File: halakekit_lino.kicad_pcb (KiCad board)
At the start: 2 copper layers, 33 x 19.3 mm, 10 parts, among them J1 HEADER_3, J2 HEADER_3, J3 HEADER_3, J4 HEADER_3, U1 BCM20737S

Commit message: Updated to ver1.1
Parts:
- C: renamed from 100u1; footprint Capacitors_SMD:C_0201 -> Capacitors_SMD:C_0603
- R: renamed from 10K1; footprint Resistors_SMD:R_0201 -> Resistors_SMD:R_0603
- moved G*** 23.5 mm to (152.3, 94.2)
- moved G*** 1.68 mm to (164.1, 110.9)
- moved J1 1.27 mm to (153.9, 109.7), turned to 270 degrees
- moved J2 1.27 mm to (179.3, 109.7), turned to 270 degrees
- moved J3 1.27 mm to (174.3, 112.2), turned to 90 degrees
- moved J4 1.27 mm to (148.9, 112.2), turned to 90 degrees
- moved R 1.17 mm to (149.5, 98.3)
- moved C 0.71 mm to (149.5, 95.3)
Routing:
- net GND: track 85.6 -> 115.3 mm, vias 4 -> 7
- net VCC: track 56.4 -> 73.2 mm, vias 3 -> 5
- net RST: track 13.6 -> 17.7 mm
- net RX: track 17.1 -> 20.9 mm
- net AIO: track 34.0 -> 37.6 mm
- net TX: track 19.9 -> 22.4 mm
- net PIO0: track 34.4 -> 33.1 mm
- net Net-(10K1-Pad2): track 10.9 -> 11.4 mm
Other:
- board size 33 x 19.3 mm -> 33 x 20.6 mm
- net class Default: trace_width 3 -> 0.1; via_dia 0.6 -> 0.5
- board text added: "CR2032"
- board text added: "ver.1.1"
- board text removed: "ver.1.0"

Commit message: Add files to order PCBA for elecrow
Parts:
- C: footprint Capacitors_SMD:C_0603 -> register_and_condensor:C_0603
- R: footprint Resistors_SMD:R_0603 -> register_and_condensor:R_0603
- moved G*** 0.24 mm to (152.4, 94.4)
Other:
- outline, holes or cut-outs redrawn
- board text added: "BCM20737S"

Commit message: Change board layout as rev 1.2
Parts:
- removed the G*** at (164.1, 110.9)
- removed J2, J3, J4: HEADER_3, simple_headers:Pin_Header_Straight_1x03_circle
- added G***: LOGO, osh-logo:osh-logo-4p3mm, F.Cu at (177.3, 100.8)
- added G***: LOGO, osh-logo:osh-logo-4p3mm, F.Cu at (174.5, 99.2)
- added G***: LOGO, osh-logo:osh-logo-3p4mm, F.Cu at (167.2, 95.2)
- added G***: LOGO, osh-logo:osh-logo-3p4mm, B.Cu at (167.4, 104.1)
- added G***: LOGO, logos:nyampass_logo_8p4mm, F.Cu at (165.1, 106.9)
- BT1: footprint CR2032_frame:BC-2001(CR2032 frame) -> CR2032_frame:BAT-HLD-001-TRCT
- J1: value HEADER_3 -> HEADER_10; footprint simple_headers:Pin_Header_Straight_1x03_circle -> simple_headers:Pin_Header_Straight_1x10
- moved G*** 17.9 mm to (165.1, 107.0), turned to 0 degrees
- moved J1 8.82 mm to (145.3, 111.4), turned to 90 degrees
- moved BT1 7.13 mm to (156.7, 98.5)
- moved R 2.24 mm to (148.5, 96.3), turned to 0 degrees
- moved C 1.31 mm to (148.5, 94.4), turned to 0 degrees
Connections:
- J1 pad 1: RST -> FWTX
- J1 pad 2: RX -> FWRX
- J1 pad 3: TX -> VCC
- U1 pad 1: PIO1 -> D1
- U1 pad 18: RX -> FWRX
- U1 pad 19: TX -> FWTX
- U1 pad 27: RST -> Net-(U1-Pad27)
- U1 pad 28: Net-(U1-Pad28) -> TX
- U1 pad 31: Net-(U1-Pad31) -> RX
- U1 pad 35: Net-(U1-Pad35) -> A1
- U1 pad 40: AIO -> A0
- U1 pad 42: PIO0 -> D0
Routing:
- net AIO: track 37.6 -> 0.00 mm, vias 1 -> 0
- net PIO1: track 33.7 -> 0.00 mm, vias 1 -> 0
- net PIO0: track 33.1 -> 0.00 mm, vias 1 -> 0
- net FWTX: track 0.00 -> 27.0 mm, vias 0 -> 1
- net D1: track 0.00 -> 25.2 mm, vias 0 -> 1
- net FWRX: track 0.00 -> 23.1 mm, vias 0 -> 1
- net D0: track 0.00 -> 18.4 mm, vias 0 -> 1
- net A1: track 0.00 -> 18.3 mm, vias 0 -> 1
- net RST: track 17.7 -> 0.00 mm, vias 1 -> 0
- net A0: track 0.00 -> 17.4 mm, vias 0 -> 1
- net VCC: track 73.2 -> 69.4 mm, vias 5 -> 3
- net TX: track 22.4 -> 23.6 mm
- net Net-(10K1-Pad2): track 11.4 -> 12.6 mm
- net GND: track 115.3 -> 115.4 mm, vias 7 -> 8
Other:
- board size 33 x 20.6 mm -> 25.5 x 20.1 mm
- net class GND added: clearance 0.1, trace_width 0.2, via_dia 0.5, via_drill 0.4
- net class VCC added: clearance 0.1, trace_width 0.2, via_dia 0.5, via_drill 0.4
- board text added: "A0 P14"
- board text added: "A1 P32"
- board text added: "D0 P26"
- board text added: "D1 D27"
- board text added: "D1 P27"
- board text added: "FW RX"
- board text added: "FW TX"
- board text added: "HaLakeKit"
- board text added: "Lino"
- board text added: "RX P2"
- board text added: "Rev 2.0"
- board text added: "TX P0"
- board text removed: "AIO0"
- board text removed: "BCM20737S"
- board text removed: "PIO0"
- board text removed: "PIO1"
- board text removed: "RST"
- board text removed: "RX"
- board text removed: "TX"
- board text removed: "ver.1.1"

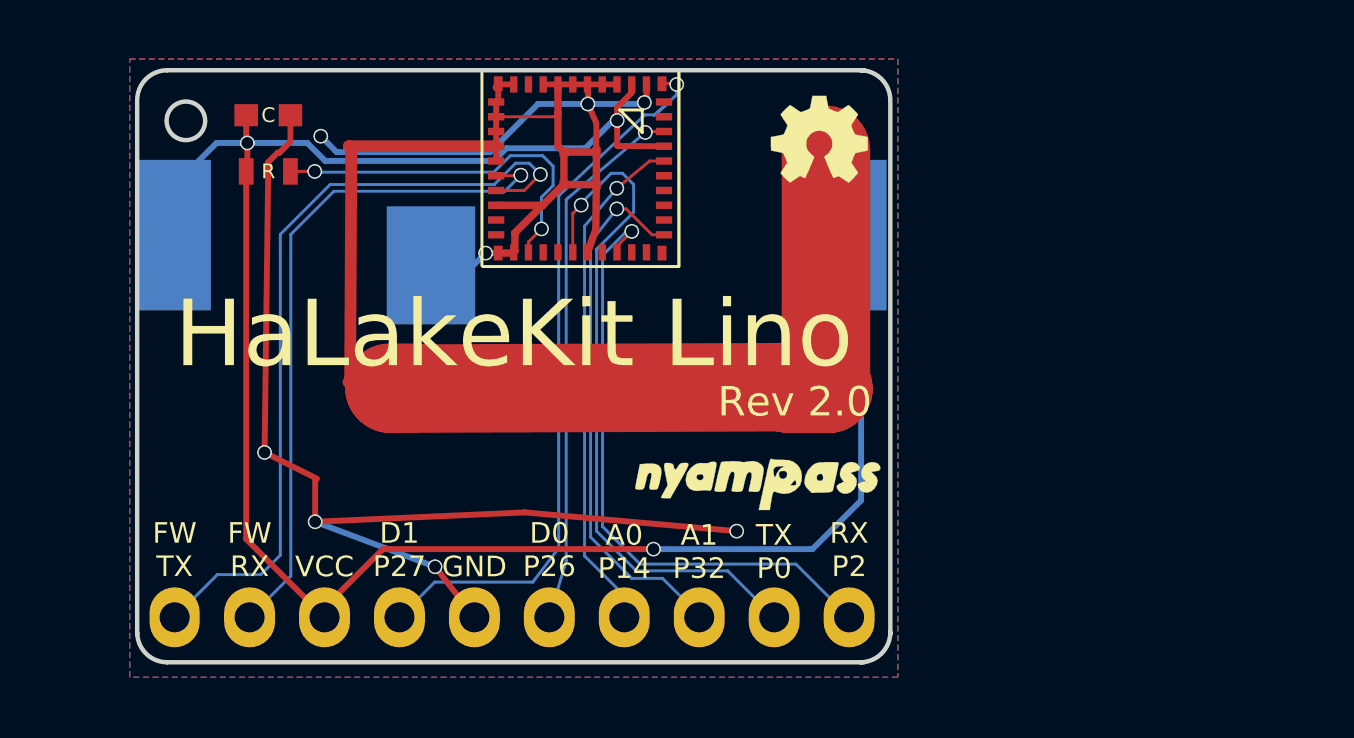
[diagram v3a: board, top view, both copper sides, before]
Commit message: Create net data with using MDBT40
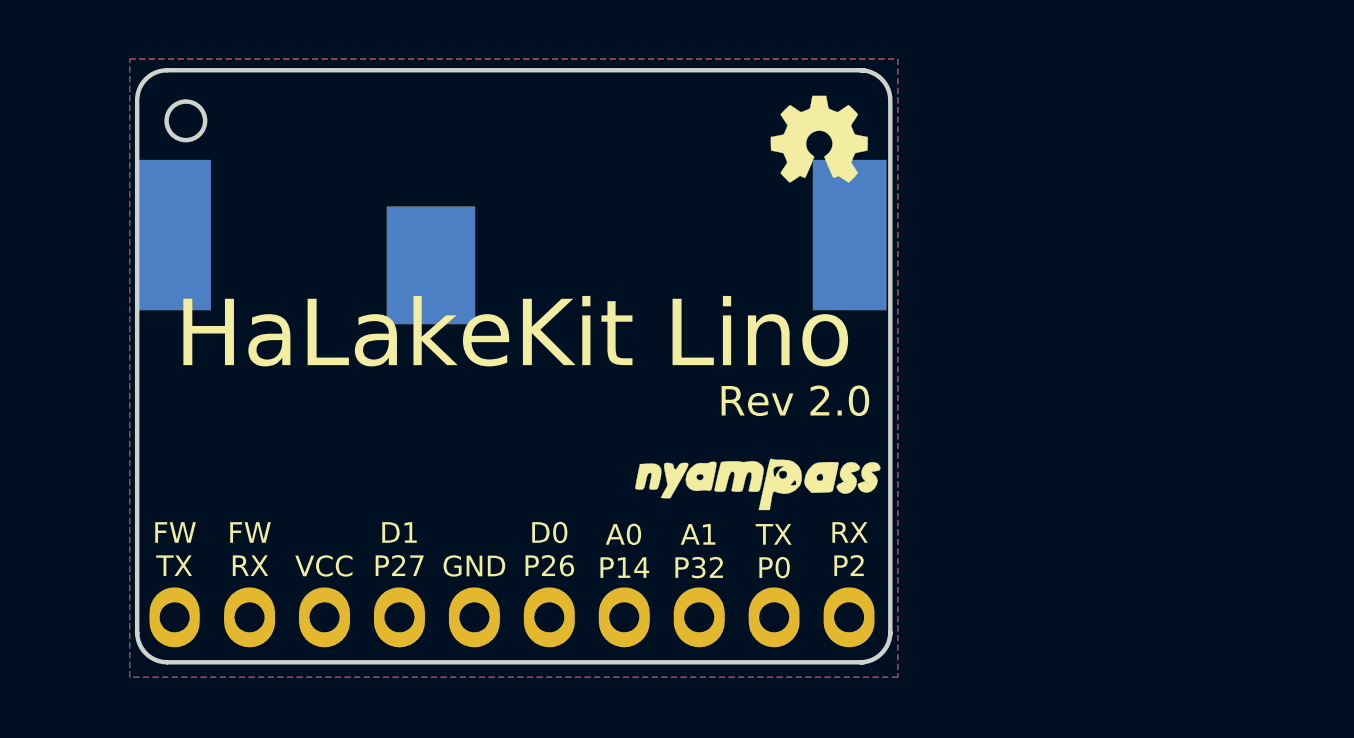
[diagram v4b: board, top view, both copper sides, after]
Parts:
- removed C: C, register_and_condensor:C_0603
- removed R: R, register_and_condensor:R_0603
- removed U1: BCM20737S, BCM20737S:BCM20737S
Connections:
- BT1 pad 1: VCC -> +3V3
- J1 pad 1: FWTX -> SWDCLK
- J1 pad 10: RX -> P4_Drain
- J1 pad 2: FWRX -> SWDIO
- J1 pad 3: VCC -> P0
- J1 pad 4: D1 -> P1
- J1 pad 6: D0 -> VCC
- J1 pad 7: A0 -> +3V3
- J1 pad 8: A1 -> P2
- J1 pad 9: TX -> P3
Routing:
- net GND: track 115.4 -> 1.44 mm, vias 8 -> 0
- net VCC: track 69.4 -> 0.00 mm, vias 3 -> 0
- net FWTX: track 27.0 -> 0.00 mm, vias 1 -> 0
- net D1: track 25.2 -> 0.00 mm, vias 1 -> 0
- net TX: track 23.6 -> 0.00 mm, vias 1 -> 0
- net FWRX: track 23.1 -> 0.00 mm, vias 1 -> 0
- net RX: track 21.1 -> 0.00 mm, vias 1 -> 0
- net D0: track 18.4 -> 0.00 mm, vias 1 -> 0
- net A1: track 18.3 -> 0.00 mm, vias 1 -> 0
- net A0: track 17.4 -> 0.00 mm, vias 1 -> 0
- net Net-(10K1-Pad2): track 12.6 -> 0.00 mm, vias 2 -> 0
- net +3V3: track 0.00 -> 4.71 mm

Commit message: Update pcb to rev3.0
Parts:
- added C1: 12pf, register_and_condensor:C_0603, F.Cu at (167.9, 98.5)
- added C2: 12pf, register_and_condensor:C_0603, F.Cu at (161.3, 98.5)
- added C3: 0.01uf, register_and_condensor:C_0603, F.Cu at (152.2, 98.5)
- added C4: 4.7uf1, register_and_condensor:C_0603, F.Cu at (150.4, 98.5)
- added C5: 0.1uf1, register_and_condensor:C_0603, F.Cu at (159.5, 98.5)
- added R1: 1K, register_and_condensor:R_0603, F.Cu at (157.8, 98.5)
- added R2: 1K, register_and_condensor:R_0603, F.Cu at (148.4, 98.5)
- added U1: MDBT40, MDBT40:MDBT40, F.Cu at (165.1, 105.8)
- added U2: NJM2870, common:SOT-23-5, F.Cu at (155.0, 98.5)
- added U3: RTF015N03, mosfet:rtf015n03, F.Cu at (145.1, 98.5)
- added Y1: Crystal, common:FC-135, F.Cu at (164.6, 98.5)
- moved G*** 69.6 mm to (105.4, 107.4)
- moved G*** 69.6 mm to (108.2, 108.9)
- moved J1 28.5 mm to (168.2, 94.4), turned to 270 degrees
- moved G*** 21.1 mm to (146.3, 103.0), turned to 180 degrees
- moved G*** 18.4 mm to (148.6, 98.7), turned to 180 degrees
- moved G*** 14.3 mm to (151.0, 109.8)
- moved BT1 9.40 mm to (156.7, 107.9), turned to 180 degrees
- moved G*** 5.46 mm to (171.7, 98.2)
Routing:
- net +3V3: track 4.71 -> 45.3 mm, vias 0 -> 2
- net GND: track 1.44 -> 30.1 mm, vias 0 -> 9
- net SWDCLK: track 0.00 -> 17.8 mm, vias 0 -> 1
- net SWDIO: track 0.00 -> 16.8 mm, vias 0 -> 1
- net P3: track 0.00 -> 16.1 mm, vias 0 -> 1
- net P0: track 0.33 -> 15.9 mm, vias 0 -> 1
- net P1: track 0.00 -> 14.3 mm, vias 0 -> 1
- net P4: track 0.00 -> 14.2 mm
- net P2: track 0.08 -> 13.9 mm, vias 0 -> 1
- net Net-(C1-Pad1): track 0.00 -> 10.4 mm
- net VCC: track 0.00 -> 7.20 mm
- net Net-(C2-Pad1): track 0.00 -> 6.30 mm
- net Net-(R1-Pad2): track 0.00 -> 4.60 mm, vias 0 -> 2
- net P4_Drain: track 0.00 -> 4.17 mm
- net Net-(C3-Pad1): track 0.00 -> 1.78 mm
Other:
- board size 25.5 x 20.1 mm -> 30.1 x 20.1 mm
- net class GND removed
- net class Power added: clearance 0.1, trace_width 0.2, via_dia 0.5, via_drill 0.4
- net class VCC removed
- board text added: "3.3"
- board text added: "P0"
- board text added: "P1"
- board text added: "P2"
- board text added: "P3"
- board text added: "P4 Drain"
- board text added: "Rev 3.0"
- board text added: "SW CLK"
- board text added: "SW DIO"
- board text added: "github.com/nyampass/halakekit_lino_pcb"
- board text removed: "A0 P14"
- board text removed: "A1 P32"
- board text removed: "D0 P26"
- board text removed: "D1 D27"
- board text removed: "D1 P27"
- board text removed: "FW RX"
- board text removed: "FW TX"
- board text removed: "HaLakeKit Lino"
- board text removed: "RX P2"
- board text removed: "Rev 2.0"
- board text removed: "TX P0"

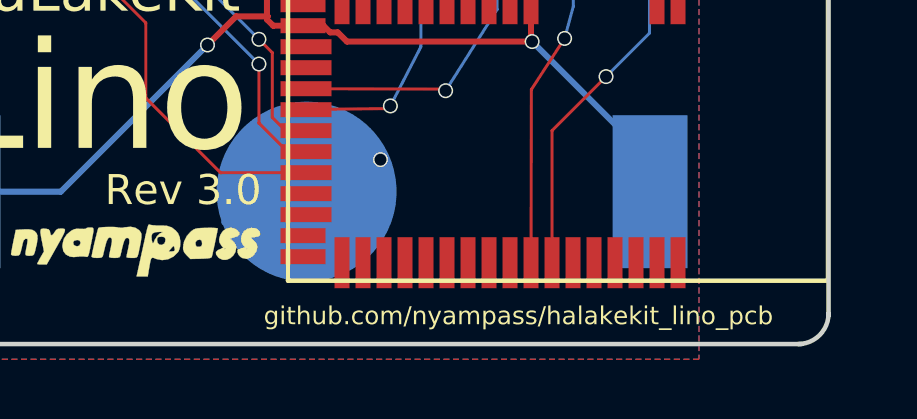
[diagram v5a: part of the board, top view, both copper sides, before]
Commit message: Change url on pcb
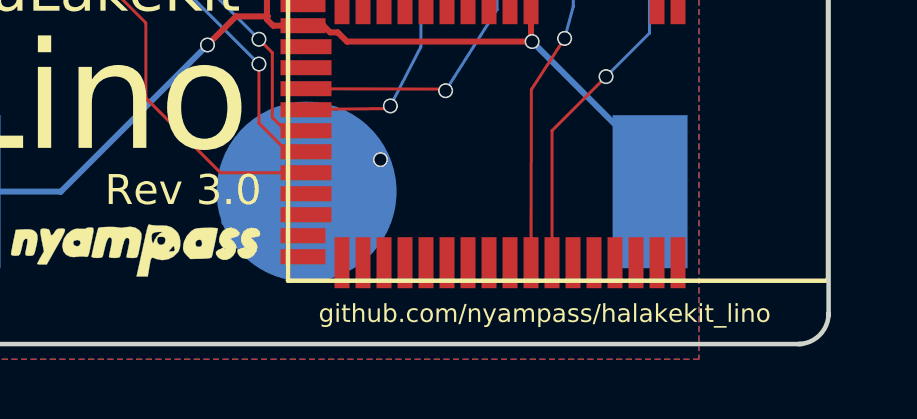
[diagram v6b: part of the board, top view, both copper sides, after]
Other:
- board text added: "github.com/nyampass/halakekit_lino"
- board text removed: "github.com/nyampass/halakekit_lino_pcb"
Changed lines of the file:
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@@
     (effects (font (size 0.7 0.7) (thickness 0.125)) (justify mirror))
   )
-  (gr_text github.com/nyampass/halakekit_lino_pcb (at 163.8046 112.014) (layer F.SilkS)
+  (gr_text github.com/nyampass/halakekit_lino (at 164.6809 111.9378) (layer F.SilkS)
     (effects (font (size 0.6 0.6) (thickness 0.15)))
   )
@@
   (segment (start 150.3934 99.2258) (end 149.8614 99.2258) (width 0.2) (layer F.Cu) (net 2))
   (segment (start 149.8614 99.2258) (end 148.3614 97.7258) (width 0.2) (layer F.Cu) (net 2))
-  (segment (start 145.2934 107.8738) (end 148.5519 107.8738) (width 0.2) (layer B.Cu) (net 13) (status 400000))
+  (segment (start 145.2934 107.8738) (end 148.5519 107.8738) (width 0.2) (layer B.Cu) (net 13))
   (segment (start 154.3939 102.0318) (end 155.4226 102.0318) (width 0.2) (layer F.Cu) (net 13))
   (segment (start 153.4414 102.9843) (end 154.3939 102.0318) (width 0.2) (layer F.Cu) (net 13))
@@
   (via (at 165.345207 102.765209) (size 0.5) (drill 0.4) (layers F.Cu B.Cu) (net 18))
   (segment (start 164.236313 104.4702) (end 165.345207 102.765209) (width 0.1) (layer F.Cu) (net 18))
-  (segment (start 156.1254 104.4418) (end 161.3251 104.4545) (width 0.1) (layer F.Cu) (net 19) (status 400000))
+  (segment (start 156.1254 104.4418) (end 161.3251 104.4545) (width 0.1) (layer F.Cu) (net 19))
   (segment (start 163.0934 101.8032) (end 163.0934 94.4118) (width 0.1) (layer B.Cu) (net 19))
   (segment (start 161.3789 104.5083) (end 163.0934 101.8032) (width 0.1) (layer B.Cu) (net 19))
   (via (at 161.3789 104.5083) (size 0.5) (drill 0.4) (layers F.Cu B.Cu) (net 19))
   (segment (start 161.3251 104.4545) (end 161.3789 104.5083) (width 0.1) (layer F.Cu) (net 19))
-  (segment (start 156.1254 105.1418) (end 159.45 105.1037) (width 0.1) (layer F.Cu) (net 20) (status 400000))
+  (segment (start 156.1254 105.1418) (end 159.45 105.1037) (width 0.1) (layer F.Cu) (net 20))
   (segment (start 160.5534 103.0478) (end 160.5534 94.4118) (width 0.1) (layer B.Cu) (net 20))
   (segment (start 159.5374 105.0163) (end 160.5534 103.0478) (width 0.1) (layer B.Cu) (net 20))
@@
   (segment (start 156.0449 105.8418) (end 155.6004 105.3973) (width 0.1) (layer F.Cu) (net 21))
   (segment (start 156.1254 105.8418) (end 156.0449 105.8418) (width 0.1) (layer F.Cu) (net 21))
-  (segment (start 156.1254 106.5418) (end 156.1099 106.5418) (width 0.1) (layer F.Cu) (net 22) (status C00000))
-  (segment (start 156.1099 106.5418) (end 155.1559 105.5878) (width 0.1) (layer F.Cu) (net 22) (status 400000))
-  (segment (start 147.8534 97.0153) (end 147.8534 94.4118) (width 0.1) (layer B.Cu) (net 22) (status 800000))
+  (segment (start 156.1254 106.5418) (end 156.1099 106.5418) (width 0.1) (layer F.Cu) (net 22))
+  (segment (start 156.1099 106.5418) (end 155.1559 105.5878) (width 0.1) (layer F.Cu) (net 22))
+  (segment (start 147.8534 97.0153) (end 147.8534 94.4118) (width 0.1) (layer B.Cu) (net 22))
   (segment (start 149.2504 98.4123) (end 147.8534 97.0153) (width 0.1) (layer B.Cu) (net 22))
   (segment (start 149.9489 98.4123) (end 149.2504 98.4123) (width 0.1) (layer B.Cu) (net 22))
